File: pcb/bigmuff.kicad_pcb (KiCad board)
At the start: 2 copper layers, 120 x 90 mm, 68 parts, among them J1 NRJ4HF, J2 NRJ4HF, J3 Conn_01x02_Pin, J4 Barrel_Jack_Switch, J5 Conn_01x02_Pin, J6 Conn_01x02_Pin, J7 Conn_01x02_Pin, J8 Conn_01x02_Pin, J9 Conn_01x02_Pin, Q1 BC549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

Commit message: update pcb
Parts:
- moved GND 5.32 mm to (113.0, 53.5), turned to -90 degrees
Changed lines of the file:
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@@
 	(footprint "Connector_PinHeader_2.54mm:PinHeader_1x02_P2.54mm_Vertical"
 		(layer "F.Cu")
-		(at 116.5 57.5)
+		(at 113 53.5 -90)
 		(descr "Through hole straight pin header, 1x02, 2.54mm pitch, single row")
 		(tags "Through hole pin header THT 1x02 2.54mm single row")
 		(property "Reference" "GND"
-			(at 0 -2.5 0)
+			(at 3 1 0)
 			(layer "F.SilkS")
 			(effects
@@
 		)
 		(property "Value" "Conn_01x02_Pin"
-			(at 0 4.92 0)
+			(at 0 4.92 90)
 			(layer "F.Fab")
 			(effects
@@
 		)
 		(property "Datasheet" ""
-			(at 0 0 0)
+			(at 0 0 90)
 			(layer "F.Fab")
 			(hide yes)
@@
 		)
 		(property "Description" "Generic connector, single row, 01x02, script generated"
-			(at 0 0 0)
+			(at 0 0 90)
 			(layer "F.Fab")
 			(hide yes)
@@
 		(attr through_hole)
 		(fp_line
+			(start -1.38 3.92)
+			(end 1.38 3.92)
+			(stroke
+				(width 0.12)
+				(type solid)
+			)
+			(layer "F.SilkS")
+		)
+		(fp_line
+			(start -1.38 1.27)
+			(end -1.38 3.92)
+			(stroke
+				(width 0.12)
+				(type solid)
+			)
+			(layer "F.SilkS")
+		)
+		(fp_line
+			(start -1.38 1.27)
+			(end 1.38 1.27)
+			(stroke
+				(width 0.12)
+				(type solid)
+			)
+			(layer "F.SilkS")
+		)
+		(fp_line
+			(start 1.38 1.27)
+			(end 1.38 3.92)
+			(stroke
+				(width 0.12)
+				(type solid)
+			)
+			(layer "F.SilkS")
+		)
+		(fp_line
+			(start -1.38 0)
+			(end -1.38 -1.38)
+			(stroke
+				(width 0.12)
+				(type solid)
+			)
+			(layer "F.SilkS")
+		)
+		(fp_line
 			(start -1.38 -1.38)
 			(end 0 -1.38)
@@
 		)
 		(fp_line
-			(start -1.38 0)
-			(end -1.38 -1.38)
-			(stroke
-				(width 0.12)
-				(type solid)
-			)
-			(layer "F.SilkS")
-		)
-		(fp_line
-			(start -1.38 1.27)
-			(end -1.38 3.92)
-			(stroke
-				(width 0.12)
-				(type solid)
-			)
-			(layer "F.SilkS")
-		)
-		(fp_line
-			(start -1.38 1.27)
-			(end 1.38 1.27)
-			(stroke
-				(width 0.12)
-				(type solid)
-			)
-			(layer "F.SilkS")
-		)
-		(fp_line
-			(start -1.38 3.92)
-			(end 1.38 3.92)
-			(stroke
-				(width 0.12)
-				(type solid)
-			)
-			(layer "F.SilkS")
-		)
-		(fp_line
-			(start 1.38 1.27)
-			(end 1.38 3.92)
-			(stroke
-				(width 0.12)
-				(type solid)
-			)
-			(layer "F.SilkS")
+			(start -1.77 4.32)
+			(end 1.77 4.32)
+			(stroke
+				(width 0.05)
+				(type solid)
+			)
+			(layer "F.CrtYd")
+		)
+		(fp_line
+			(start 1.77 4.32)
+			(end 1.77 -1.77)
+			(stroke
+				(width 0.05)
+				(type solid)
+			)
+			(layer "F.CrtYd")
 		)
 		(fp_line
@@
 		)
 		(fp_line
-			(start -1.77 4.32)
-			(end 1.77 4.32)
-			(stroke
-				(width 0.05)
-				(type solid)
-			)
-			(layer "F.CrtYd")
-		)
-		(fp_line
 			(start 1.77 -1.77)
 			(end -1.77 -1.77)
@@
 		)
 		(fp_line
-			(start 1.77 4.32)
-			(end 1.77 -1.77)
-			(stroke
-				(width 0.05)
-				(type solid)
-			)
-			(layer "F.CrtYd")
+			(start -1.27 3.81)
+			(end -1.27 -0.635)
+			(stroke
+				(width 0.1)
+				(type solid)
+			)
+			(layer "F.Fab")
+		)
+		(fp_line
+			(start 1.27 3.81)
+			(end -1.27 3.81)
+			(stroke
+				(width 0.1)
+				(type solid)
+			)
+			(layer "F.Fab")
 		)
 		(fp_line
@@
 		)
 		(fp_line
-			(start -1.27 3.81)
-			(end -1.27 -0.635)
-			(stroke
-				(width 0.1)
-				(type solid)
-			)
-			(layer "F.Fab")
-		)
-		(fp_line
 			(start -0.635 -1.27)
 			(end 1.27 -1.27)
@@
 			(layer "F.Fab")
 		)
-		(fp_line
-			(start 1.27 3.81)
-			(end -1.27 3.81)
-			(stroke
-				(width 0.1)
-				(type solid)
-			)
-			(layer "F.Fab")
-		)
 		(fp_text user "${REFERENCE}"
-			(at 0 1.27 90)
+			(at 0 1.27 0)
 			(layer "F.Fab")
 			(effects
@@
 		)
 		(pad "1" thru_hole rect
-			(at 0 0)
+			(at 0 0 270)
 			(size 1.7 1.7)
 			(drill 1)
@@
 		)
 		(pad "2" thru_hole circle
-			(at 0 2.54)
+			(at 0 2.54 270)
 			(size 1.7 1.7)
 			(drill 1)

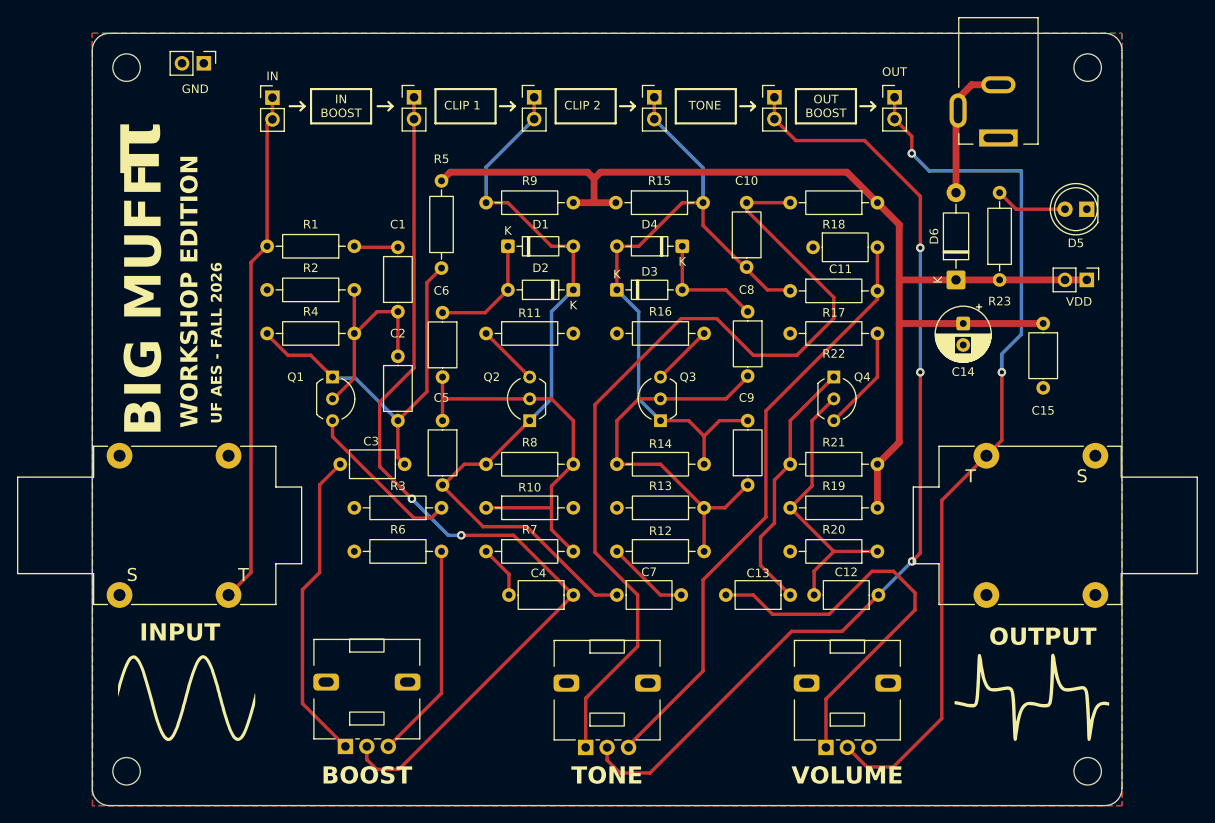
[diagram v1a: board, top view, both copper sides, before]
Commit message: added 3d models
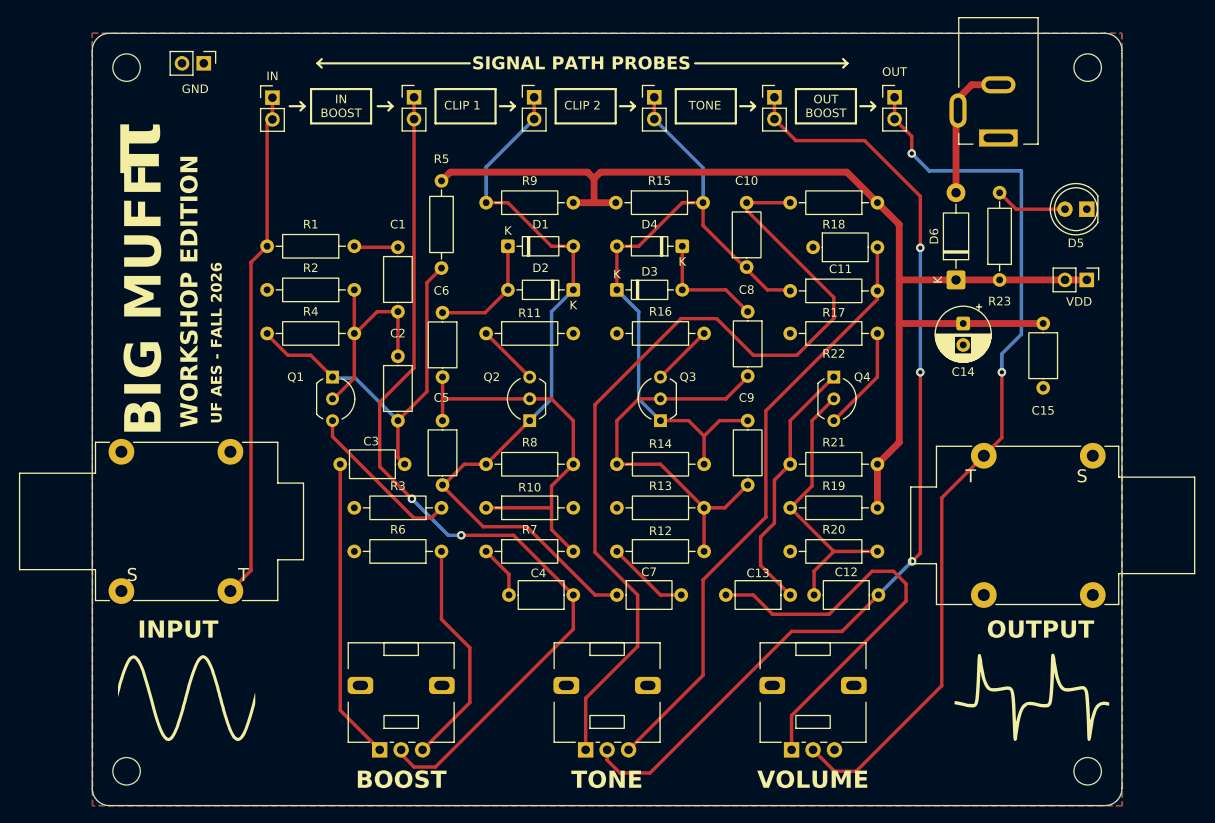
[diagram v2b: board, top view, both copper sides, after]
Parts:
- moved RV1 4.02 mm to (133.5, 133.5)
- moved RV3 4.01 mm to (181.5, 133.5)
- moved J1 0.51 mm to (116.1, 115.0)
- moved J2 0.30 mm to (203.9, 99.2)
- moved RV2 0.28 mm to (157.5, 133.5)
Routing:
- net BOOST_OUT: track 107.9 -> 105.3 mm
- net OUT: track 102.9 -> 105.0 mm
- net Net-(R6-Pad1): track 25.3 -> 26.8 mm
- net Net-(C13-Pad2): track 48.4 -> 49.5 mm
- net Net-(C3-Pad2): track 36.8 -> 35.8 mm
- net Net-(C11-Pad2): track 70.3 -> 71.1 mm
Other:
- board text added: "SIGNAL PATH PROBES"

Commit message: Passed ERC / DRC - ready for gerbers
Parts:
- removed GND, VDD: Conn_01x02_Pin, Connector_PinHeader_2.54mm:PinHeader_1x02_P2.54mm_Vertical
- removed REF** (x4): MountingHole_3.2mm_M3, MountingHole:MountingHole_3.2mm_M3
- added G***: LOGO, LOGO, F.Cu at (214.5, 75.0)
- added G***: LOGO, LOGO, F.Cu at (215.0, 59.5)
- added H1: MountingHole, MountingHole:MountingHole_3.2mm_M3, F.Cu at (104.0, 54.0)
- added H2: MountingHole, MountingHole:MountingHole_3.2mm_M3, F.Cu at (216.0, 54.0)
- added H3: MountingHole, MountingHole:MountingHole_3.2mm_M3, F.Cu at (216.0, 136.0)
- added H4: MountingHole, MountingHole:MountingHole_3.2mm_M3, F.Cu at (104.0, 136.0)
- added J10: Conn_01x02_Pin, Connector_PinHeader_2.54mm:PinHeader_1x02_P2.54mm_Vertical, F.Cu at (215.9, 78.7)
- added J11: Conn_01x02_Pin, Connector_PinHeader_2.54mm:PinHeader_1x02_P2.54mm_Vertical, F.Cu at (115.0, 55.0)
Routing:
- net Net-(C3-Pad2): track 35.8 -> 35.2 mm
- net IN: track 59.9 -> 60.4 mm
- net Net-(C11-Pad2): track 71.1 -> 70.6 mm
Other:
- board text added: "9V"
- board text added: "GND"
- board text added: "VDD"
